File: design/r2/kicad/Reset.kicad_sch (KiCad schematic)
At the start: 12 parts, among them IC15 555N

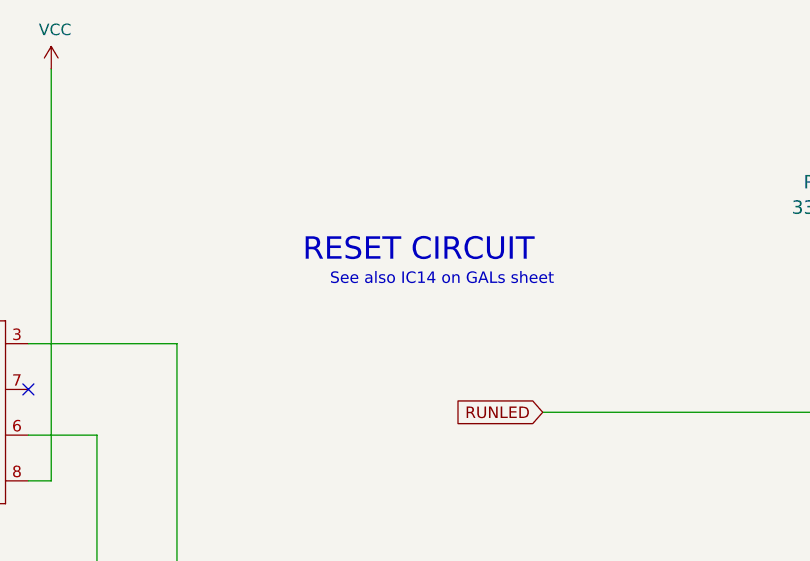
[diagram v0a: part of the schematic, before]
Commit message: Fix outdated IC14 reference
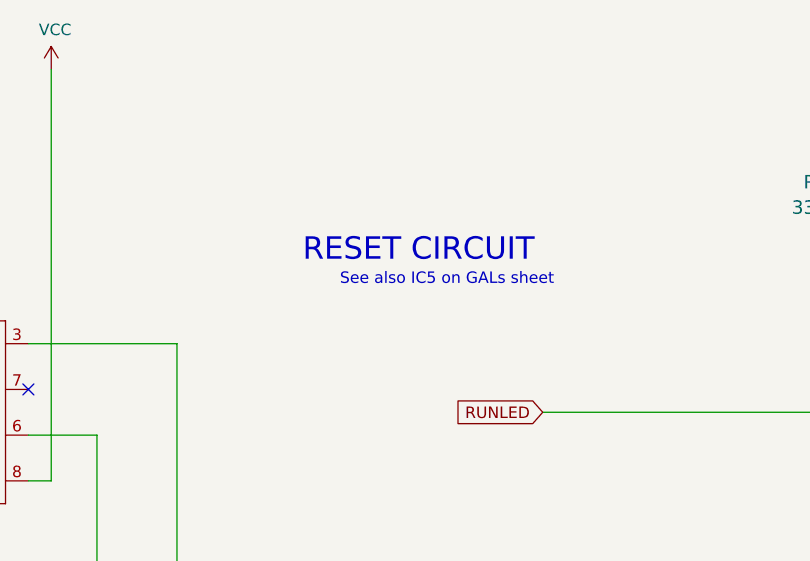
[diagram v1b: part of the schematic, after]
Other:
- note added: "See also IC5 on GALs sheet"
- note removed: "See also IC14 on GALs sheet"
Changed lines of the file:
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@@
     (stroke (width 0) (type default) (color 0 0 0 0))
   )
-  (text "See also IC14 on GALs sheet" (at 156.21 80.01 180)
+  (text "See also IC5 on GALs sheet" (at 156.21 80.01 180)
     (effects (font (size 1.27 1.27)) (justify right bottom))
   )

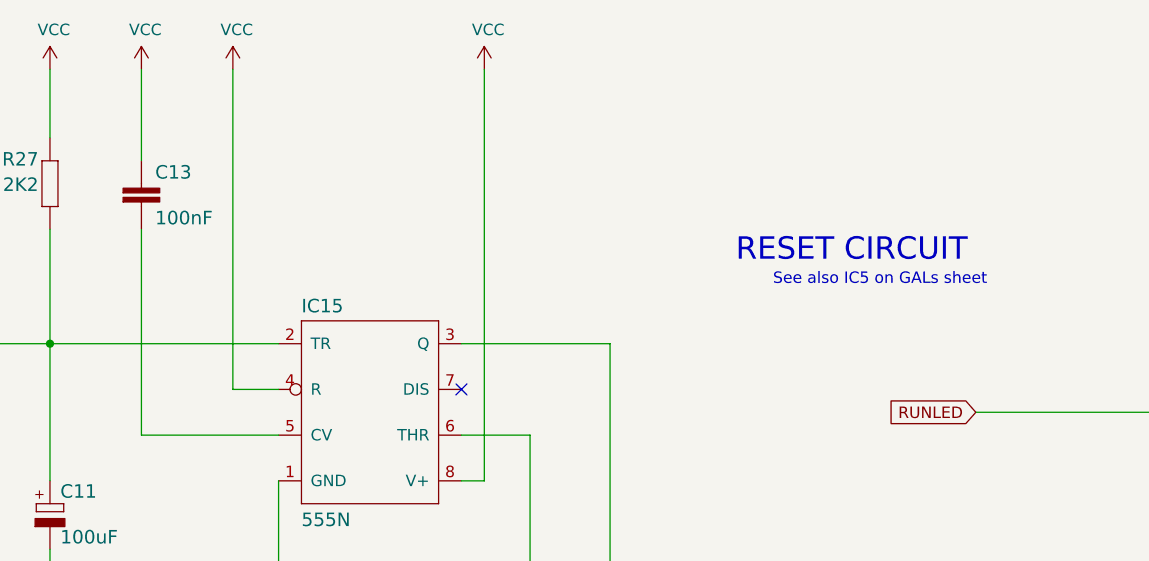
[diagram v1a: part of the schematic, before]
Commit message: Use reference instead of hardcoding
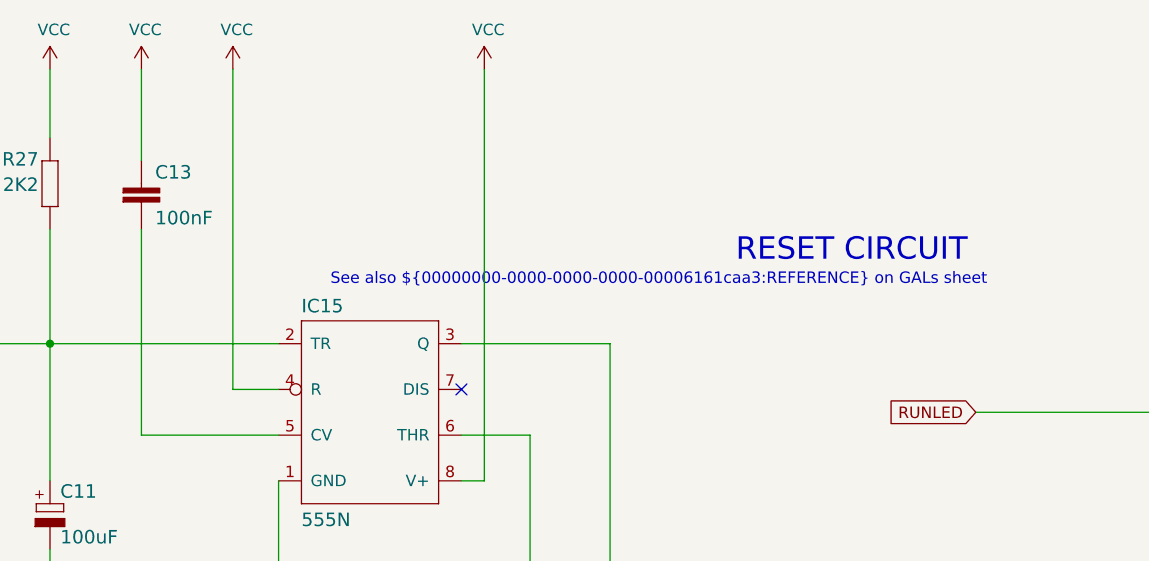
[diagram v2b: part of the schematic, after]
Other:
- note added: "See also ${00000000-0000-0000-0000-00006161caa3:REFERENCE} on GALs sheet"
- note removed: "See also IC5 on GALs sheet"
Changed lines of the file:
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@@
     (stroke (width 0) (type default) (color 0 0 0 0))
   )
-  (text "See also IC5 on GALs sheet" (at 156.21 80.01 180)
+  (text "See also ${00000000-0000-0000-0000-00006161caa3:REFERENCE} on GALs sheet"
+    (at 156.21 80.01 0)
     (effects (font (size 1.27 1.27)) (justify right bottom))
   )
